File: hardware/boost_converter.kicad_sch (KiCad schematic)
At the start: 13 parts, among them J2 Conn_01x02_Pin, U3 SparkFun_LiPower, U4 TPS61200DRC

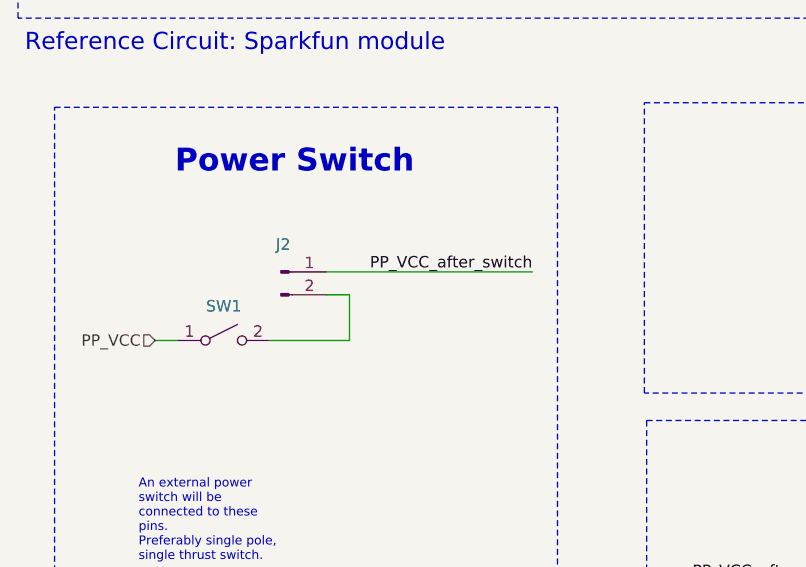
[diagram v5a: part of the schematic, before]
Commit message: Changed the J2 connector for the same one as the J1
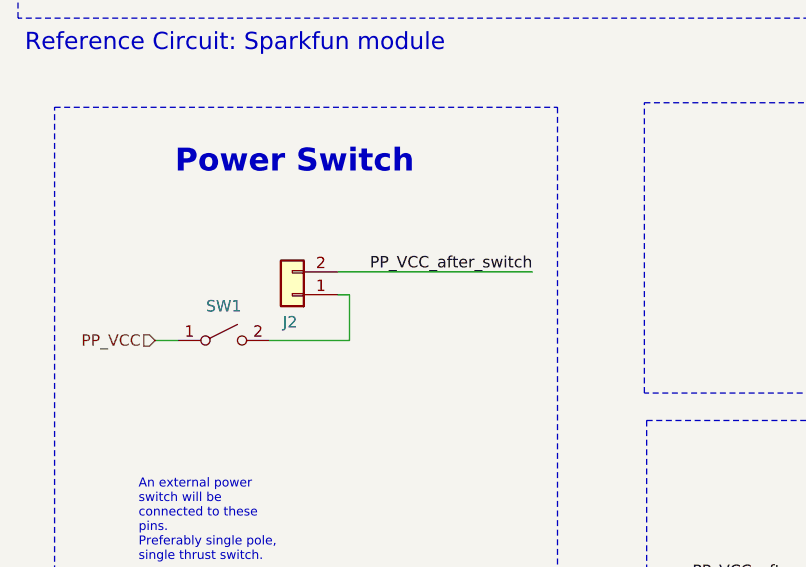
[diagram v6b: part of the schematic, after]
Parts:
- J2: footprint Connector_PinHeader_2.54mm:PinHeader_1x02_P2.54mm_Vertical -> kitchen_timer:JST_XH_1x02_P2.54mm_Vertical; symbol Connector:Conn_01x02_Pin -> Connector_Generic:Conn_01x02; now in the parts list
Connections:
- net PP_VCC_after_switch: now also J2.2 (Pin_2); no longer J2.1 (Pin_1)
- net at SW1.2 (B): now also J2.1 (Pin_1); no longer J2.2 (Pin_2)
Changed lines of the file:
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@@
-	(wire
-		(pts
-			(xy 73.66 80.01) (xy 50.8 80.01)
-		)
-		(stroke
-			(width 0)
-			(type default)
-		)
-	)
 	(wire
 		(pts
@@
 	(wire
 		(pts
-			(xy 53.34 82.55) (xy 50.8 82.55)
-		)
-		(stroke
-			(width 0)
-			(type default)
-		)
-	)
-	(wire
-		(pts
 			(xy 130.81 85.09) (xy 135.89 85.09)
 		)
@@
 	(wire
 		(pts
+			(xy 52.07 80.01) (xy 73.66 80.01)
+		)
+		(stroke
+			(width 0)
+			(type default)
+		)
+	)
+	(wire
+		(pts
 			(xy 119.38 129.54) (xy 119.38 133.35)
 		)
@@
 		(pts
 			(xy 147.32 139.7) (xy 147.32 143.51)
+		)
+		(stroke
+			(width 0)
+			(type default)
+		)
+	)
+	(wire
+		(pts
+			(xy 52.07 82.55) (xy 53.34 82.55)
 		)
 		(stroke
@@
 	)
 	(symbol
-		(lib_id "Connector:Conn_01x02_Pin")
-		(at 45.72 80.01 0)
+		(lib_id "Connector_Generic:Conn_01x02")
+		(at 46.99 82.55 180)
 		(unit 1)
 		(exclude_from_sim no)
-		(in_bom no)
+		(in_bom yes)
 		(on_board yes)
 		(dnp no)
 		(property "Reference" "J2"
-			(at 45.974 76.962 0)
+			(at 46.736 85.598 0)
 			(effects
 				(font
@@
 		)
 		(property "Value" "Conn_01x02_Pin"
-			(at 52.832 85.344 0)
-			(effects
-				(font
-					(size 1.27 1.27)
-				)
-				(hide yes)
-			)
-		)
-		(property "Footprint" "Connector_PinHeader_2.54mm:PinHeader_1x02_P2.54mm_Vertical"
-			(at 45.72 80.01 0)
+			(at 39.878 77.216 0)
+			(effects
+				(font
+					(size 1.27 1.27)
+				)
+				(hide yes)
+			)
+		)
+		(property "Footprint" "kitchen_timer:JST_XH_1x02_P2.54mm_Vertical"
+			(at 46.99 82.55 0)
 			(effects
 				(font
@@
 		)
 		(property "Datasheet" "~"
-			(at 45.72 80.01 0)
-			(effects
-				(font
-					(size 1.27 1.27)
-				)
-				(hide yes)
-			)
-		)
-		(property "Description" "Generic connector, single row, 01x02, script generated"
-			(at 45.72 80.01 0)
+			(at 46.99 82.55 0)
+			(effects
+				(font
+					(size 1.27 1.27)
+				)
+				(hide yes)
+			)
+		)
+		(property "Description" "Generic connector, single row, 01x02, script generated (kicad-library-utils/schlib/autogen/connector/)"
+			(at 46.99 82.55 0)
 			(effects
 				(font
@@
 		)
 		(property "Supplier Unit Price" "~"
-			(at 45.72 80.01 0)
+			(at 46.99 82.55 0)
 			(effects
 				(font
@@
 		)
 		(property "Part Num" ""
-			(at 45.72 80.01 0)
+			(at 46.99 82.55 0)
 			(effects
 				(font
@@
 		)
 		(property "Package" "~"
-			(at 45.72 80.01 0)
+			(at 46.99 82.55 0)
 			(effects
 				(font
@@
 		)
 		(property "Manuf. Name" "~"
-			(at 45.72 80.01 0)
+			(at 46.99 82.55 0)
 			(effects
 				(font
@@
 		)
 		(property "Manuf. Part #" "~"
-			(at 45.72 80.01 0)
+			(at 46.99 82.55 0)
 			(effects
 				(font
@@
 		)
 		(property "Supplier Name" "~"
-			(at 45.72 80.01 0)
+			(at 46.99 82.55 0)
 			(effects
 				(font
@@
 		)
 		(property "Supplier Part #" "~"
-			(at 45.72 80.01 0)
+			(at 46.99 82.55 0)
 			(effects
 				(font
@@
 		)
 		(property "Supplier Link" "~"
-			(at 45.72 80.01 0)
+			(at 46.99 82.55 0)
 			(effects
 				(font
@@
 		)
 		(property "Manufacturer_Name" ""
-			(at 45.72 80.01 0)
+			(at 46.99 82.55 0)
 			(effects
 				(font
@@
 		)
 		(property "Manufacturer_Part_Number" ""
-			(at 45.72 80.01 0)
+			(at 46.99 82.55 0)
 			(effects
 				(font
@@
 		)
 		(property "Mouser Part Number" ""
-			(at 45.72 80.01 0)
+			(at 46.99 82.55 0)
 			(effects
 				(font
@@
 		)
 		(property "Mouser Price/Stock" ""
-			(at 45.72 80.01 0)
-			(effects
-				(font
+			(at 46.99 82.55 0)
+			(effects
+				(font

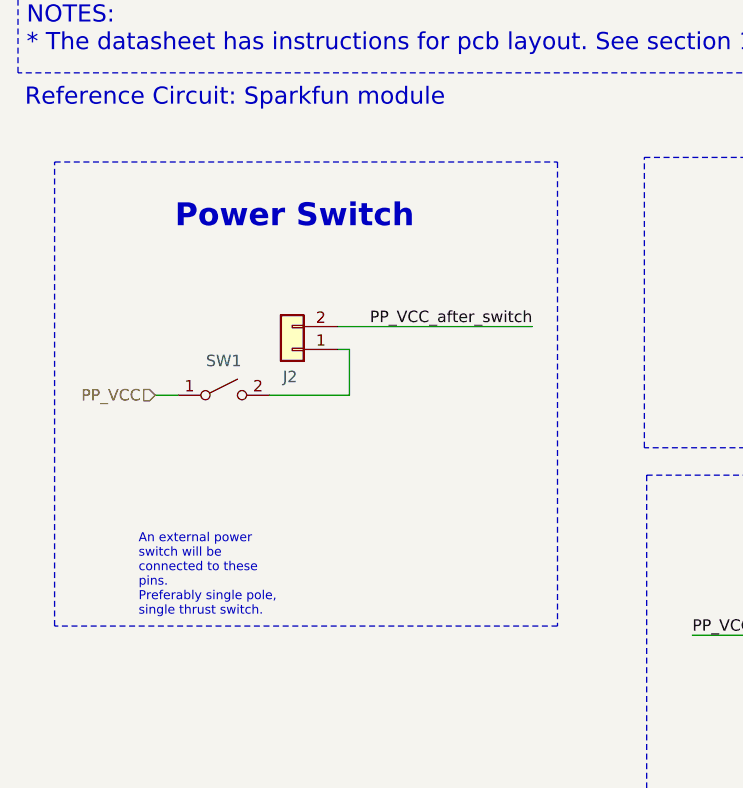
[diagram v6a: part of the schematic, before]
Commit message: Removed the power switch symbol form the schematic. It was adding an undefined net and hiding the connection between the boost converter and the power path.
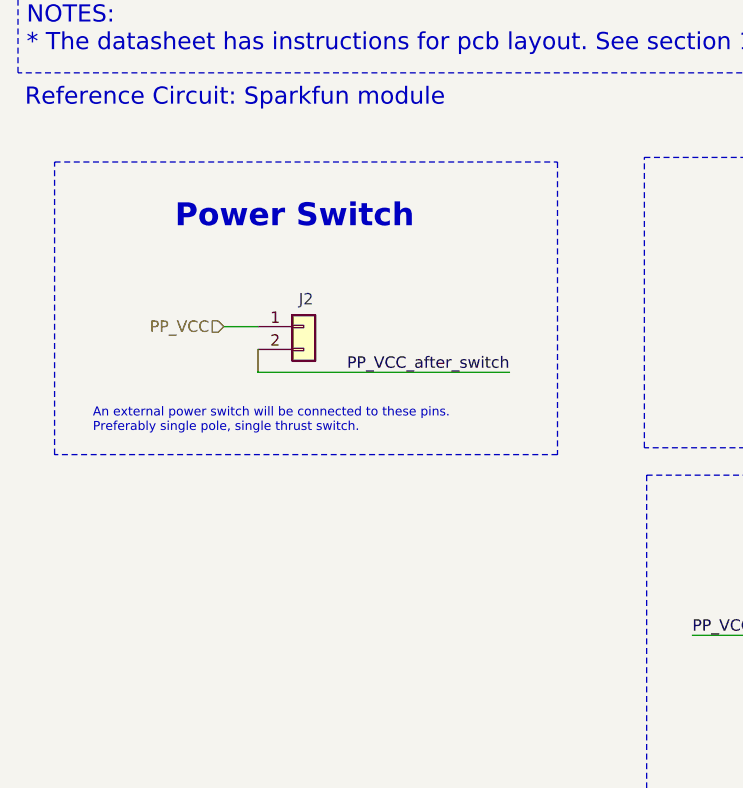
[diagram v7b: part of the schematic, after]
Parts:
- removed SW1: ~, ~, symbol Switch:SW_SPST
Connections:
- net PP_VCC: now also J2.1 (Pin_1)
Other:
- moved on the sheet: J2

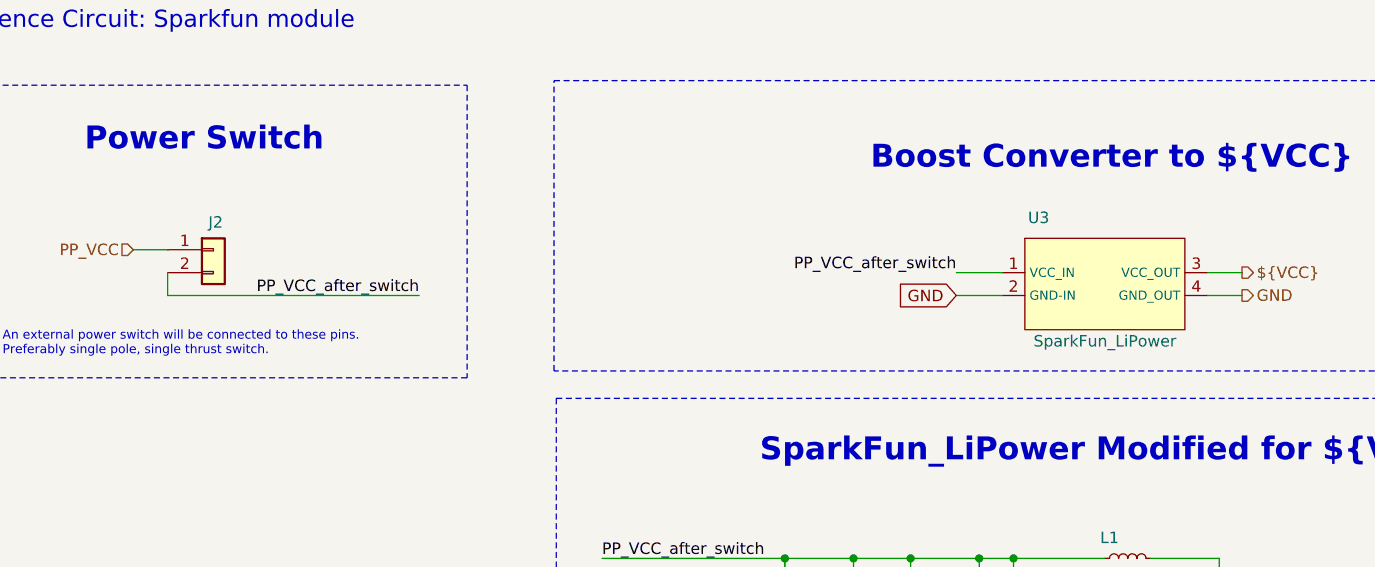
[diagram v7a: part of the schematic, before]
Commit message: Reviewed the Fields Table and marked all components that should not be populated. Then I runned rules check in the schematic and PCB
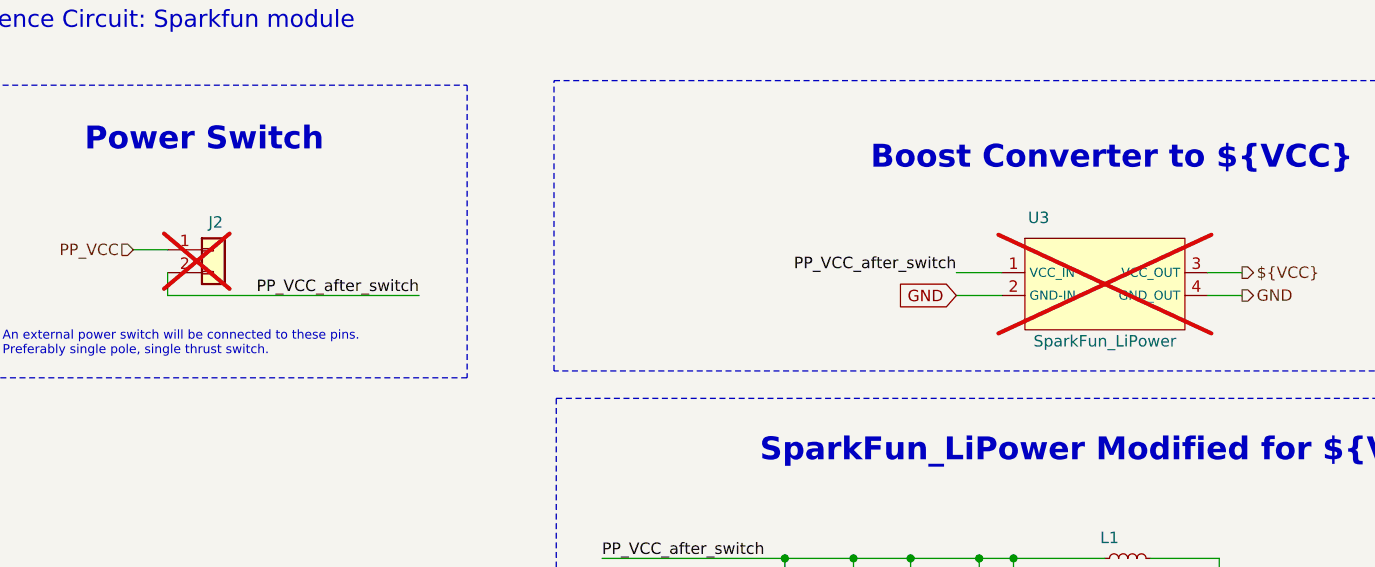
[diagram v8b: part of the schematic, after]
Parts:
- J2: now not fitted; now left out of the parts list
- U3: now not fitted
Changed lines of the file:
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@@
 		(unit 1)
 		(exclude_from_sim no)
-		(in_bom yes)
+		(in_bom no)
 		(on_board yes)
-		(dnp no)
+		(dnp yes)
 		(property "Reference" "J2"
 			(at 48.514 76.962 0)
@@
 		(in_bom no)
 		(on_board yes)
-		(dnp no)
+		(dnp yes)
 		(property "Reference" "U3"
 			(at 139.954 76.454 0)
